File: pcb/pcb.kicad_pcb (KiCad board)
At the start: 2 copper layers, 37 x 23.5 mm, 7 parts

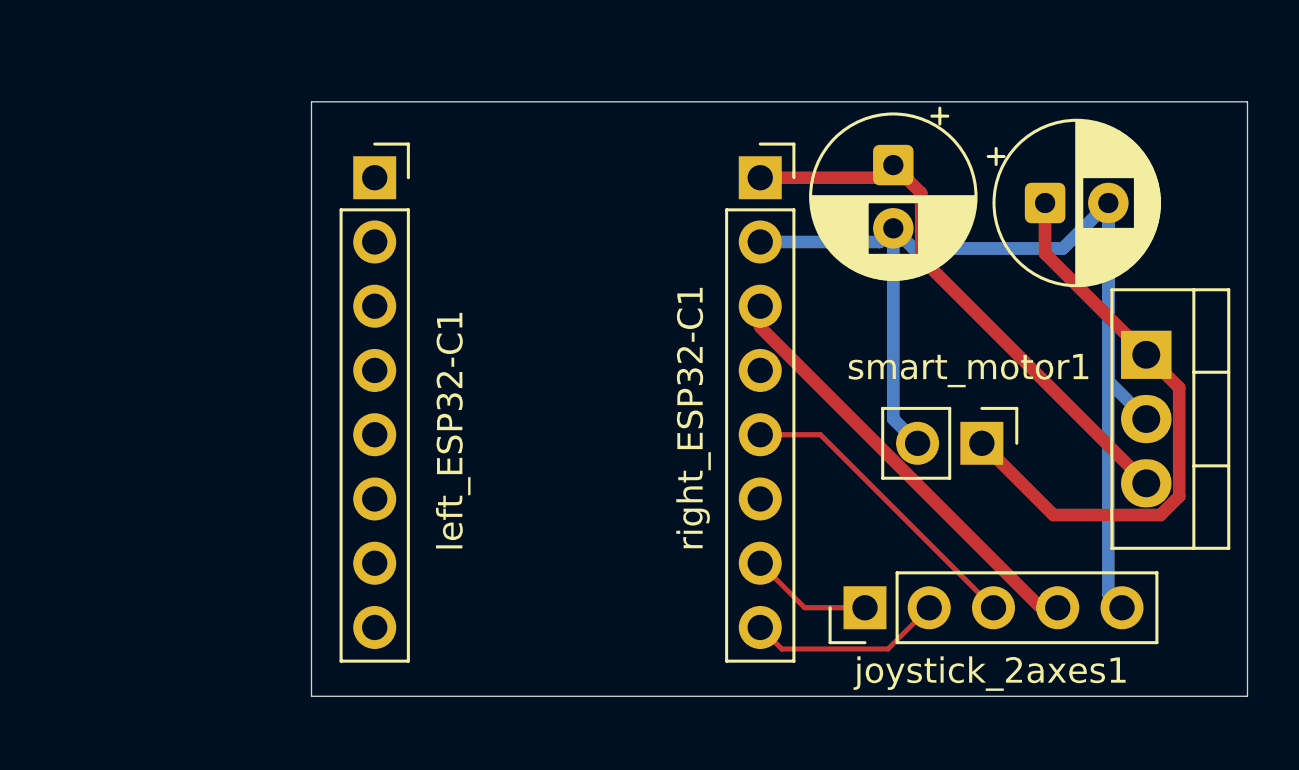
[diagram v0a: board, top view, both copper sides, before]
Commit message: added ground plane on front and back of pcb
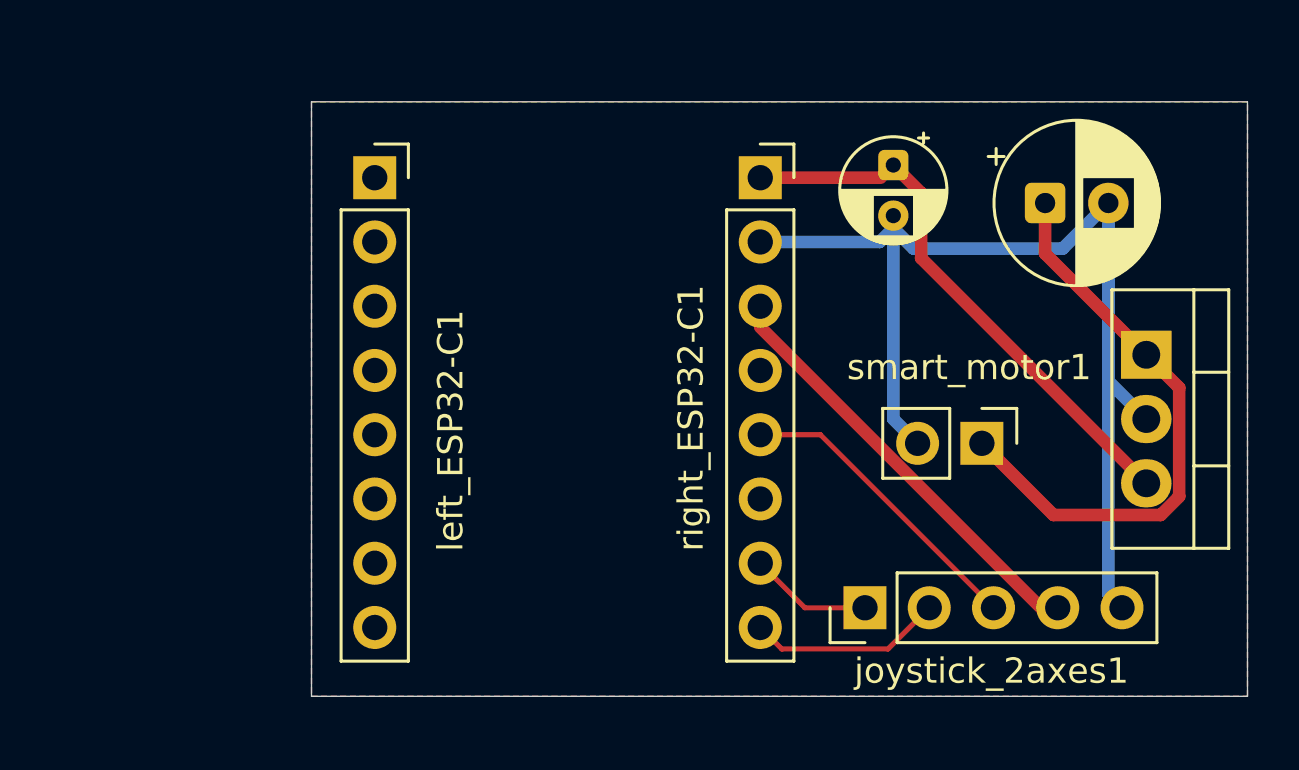
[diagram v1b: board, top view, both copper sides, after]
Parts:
- output_c1: renamed from output_c_pol1; footprint Capacitor_THT:CP_Radial_D6.3mm_P2.50mm -> Capacitor_THT:CP_Radial_D4.0mm_P2.00mm
- renumbered input_c_pol1 to input_c1
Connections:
- net Net-(joystick_2axes1-5V) renamed /3V3
- net Net-(joystick_2axes1-GND) renamed GND
- net Net-(joystick_2axes1-Rx) renamed /RX
- net Net-(joystick_2axes1-Ry) renamed /SW
- net Net-(joystick_2axes1-SW) renamed /RY
- net Net-(right_ESP32-C1-5V) renamed /5V0
- net Net-(smart_motor1-7V4) renamed /7V4
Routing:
- added copper zone on B.Cu, net GND
- added copper zone on F.Cu, net GND

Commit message: new pcb with custom footprint
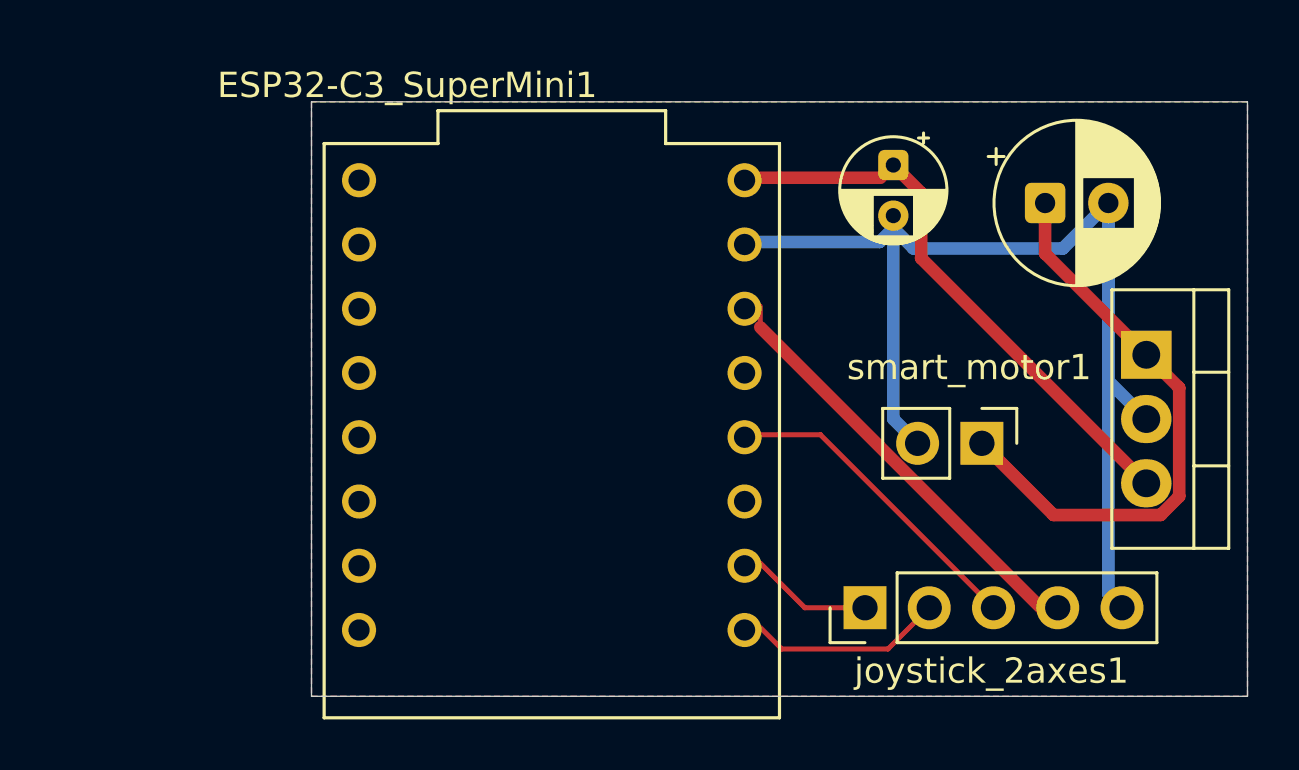
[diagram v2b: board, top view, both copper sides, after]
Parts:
- removed left_ESP32-C1, right_ESP32-C1: Conn_01x08, Connector_PinSocket_2.54mm:PinSocket_1x08_P2.54mm_Vertical
- added ESP32-C3_SuperMini1: ESP32-C3_SUPERMINI_TH, ESP32-C3_SUPERMINI_TH:MODULE_ESP32-C3_SUPERMINI_TH, F.Cu at (107.0, 110.0)
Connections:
- joystick_2axes1 pad 1: /RY -> /SW
- joystick_2axes1 pad 2: /SW -> /RY
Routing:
- net /SW: track 7.71 -> 4.87 mm
- net /RY: track 4.87 -> 7.71 mm

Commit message: added rounded edges, mounting holes and legend on pcb
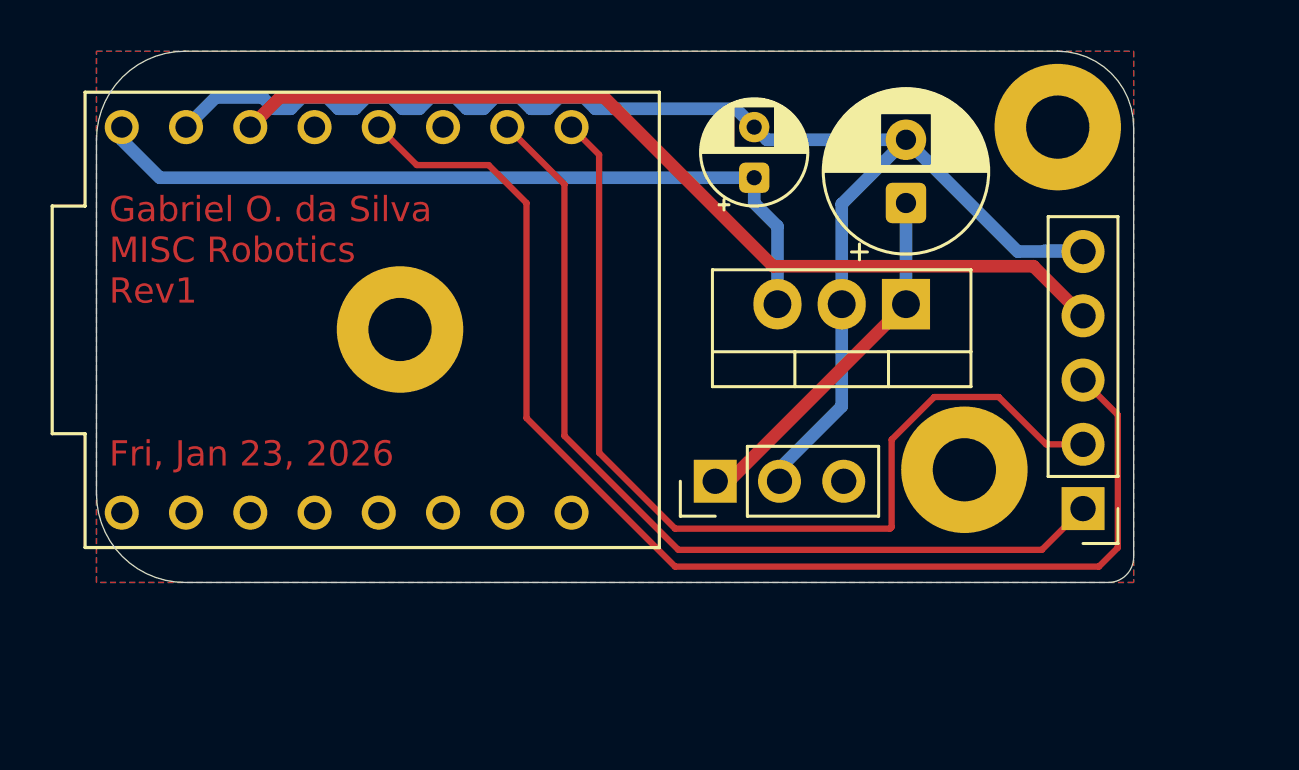
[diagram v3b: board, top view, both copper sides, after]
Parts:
- added H1: MountingHole_Pad, MountingHole:MountingHole_2.5mm_Pad, F.Cu at (101.0, 106.0)
- added H2: MountingHole_Pad, MountingHole:MountingHole_2.5mm_Pad, F.Cu at (127.0, 98.0)
- added H3: MountingHole_Pad, MountingHole:MountingHole_2.5mm_Pad, F.Cu at (123.3, 111.5)
- smart_motor1: value Conn_01x02 -> Conn_01x03; footprint Connector_PinHeader_2.54mm:PinHeader_1x02_P2.54mm_Vertical -> Connector_PinHeader_2.54mm:PinHeader_1x03_P2.54mm_Vertical
- moved smart_motor1 10.6 mm to (113.5, 112.0), turned to 90 degrees
- moved volt_reg1 9.71 mm to (121.0, 105.0), turned to 180 degrees
- moved joystick_2axes1 9.47 mm to (128.0, 113.1), turned to 180 degrees
- moved ESP32-C3_SuperMini1 8.34 mm to (99.9, 105.6), turned to 90 degrees
- moved output_c1 5.52 mm to (115.0, 100.0), turned to 90 degrees
- moved input_c1 5.50 mm to (121.0, 101.0), turned to 90 degrees
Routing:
- net /RX: track 12.1 -> 48.9 mm
- net /SW: track 4.87 -> 36.2 mm
- net /RY: track 7.71 -> 38.6 mm
- net /3V3: track 17.2 -> 37.0 mm
- net /5V0: track 22.2 -> 31.5 mm
- net /7V4: track 23.1 -> 14.4 mm
- net GND: track 49.3 -> 57.4 mm
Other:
- board size 37 x 23.5 mm -> 41 x 21 mm
- board text added: "Gabriel O. da Silva MISC Robotics Rev1 Fri, Jan 23, 2026"

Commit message: added pin socket rows for teleop pcb
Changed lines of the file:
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@@
 			(drillshape 0)
 			(scaleselection 1)
-			(outputdirectory "drill/")
+			(outputdirectory "gerber")
 		)
 	)
@@
 	(gr_text "Gabriel O. da Silva\nMISC Robotics\nRev1\n\n\n\nFri, Jan 23, 2026"
 		(at 89.5 111.5 0)
-		(layer "F.Cu")
+		(layer "F.Mask")
 		(effects
 			(font
